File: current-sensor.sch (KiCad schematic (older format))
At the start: 36 parts, among them J1 ‎0197134001‎, J2 ‎0197134001‎, J3 0731000105, J4 Molex_SL_01x02_Male, J5 Molex_SL_01x02_Male, SW1 PN12Sxxx03QE, SW2 OS103011MA7QP1, SW3 OS103011MA7QP1, U1 ACS730xLCTR-40AB, U2 AD8616xRM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

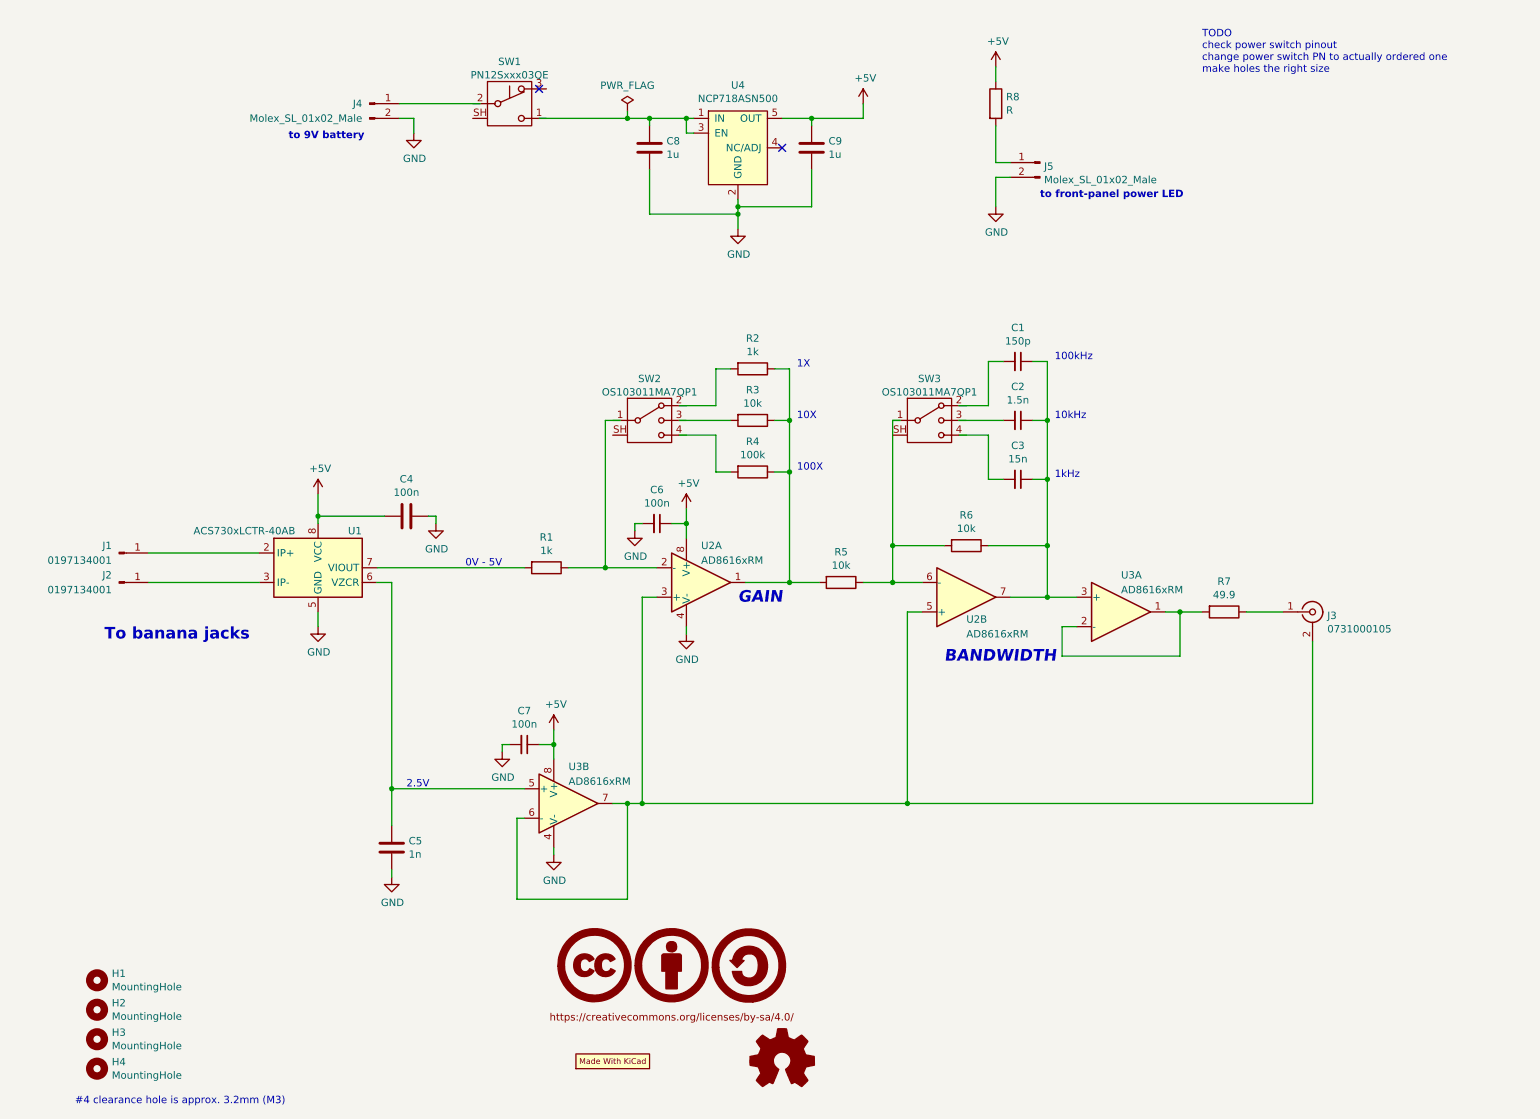
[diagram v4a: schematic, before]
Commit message: complete basic schematic & routing
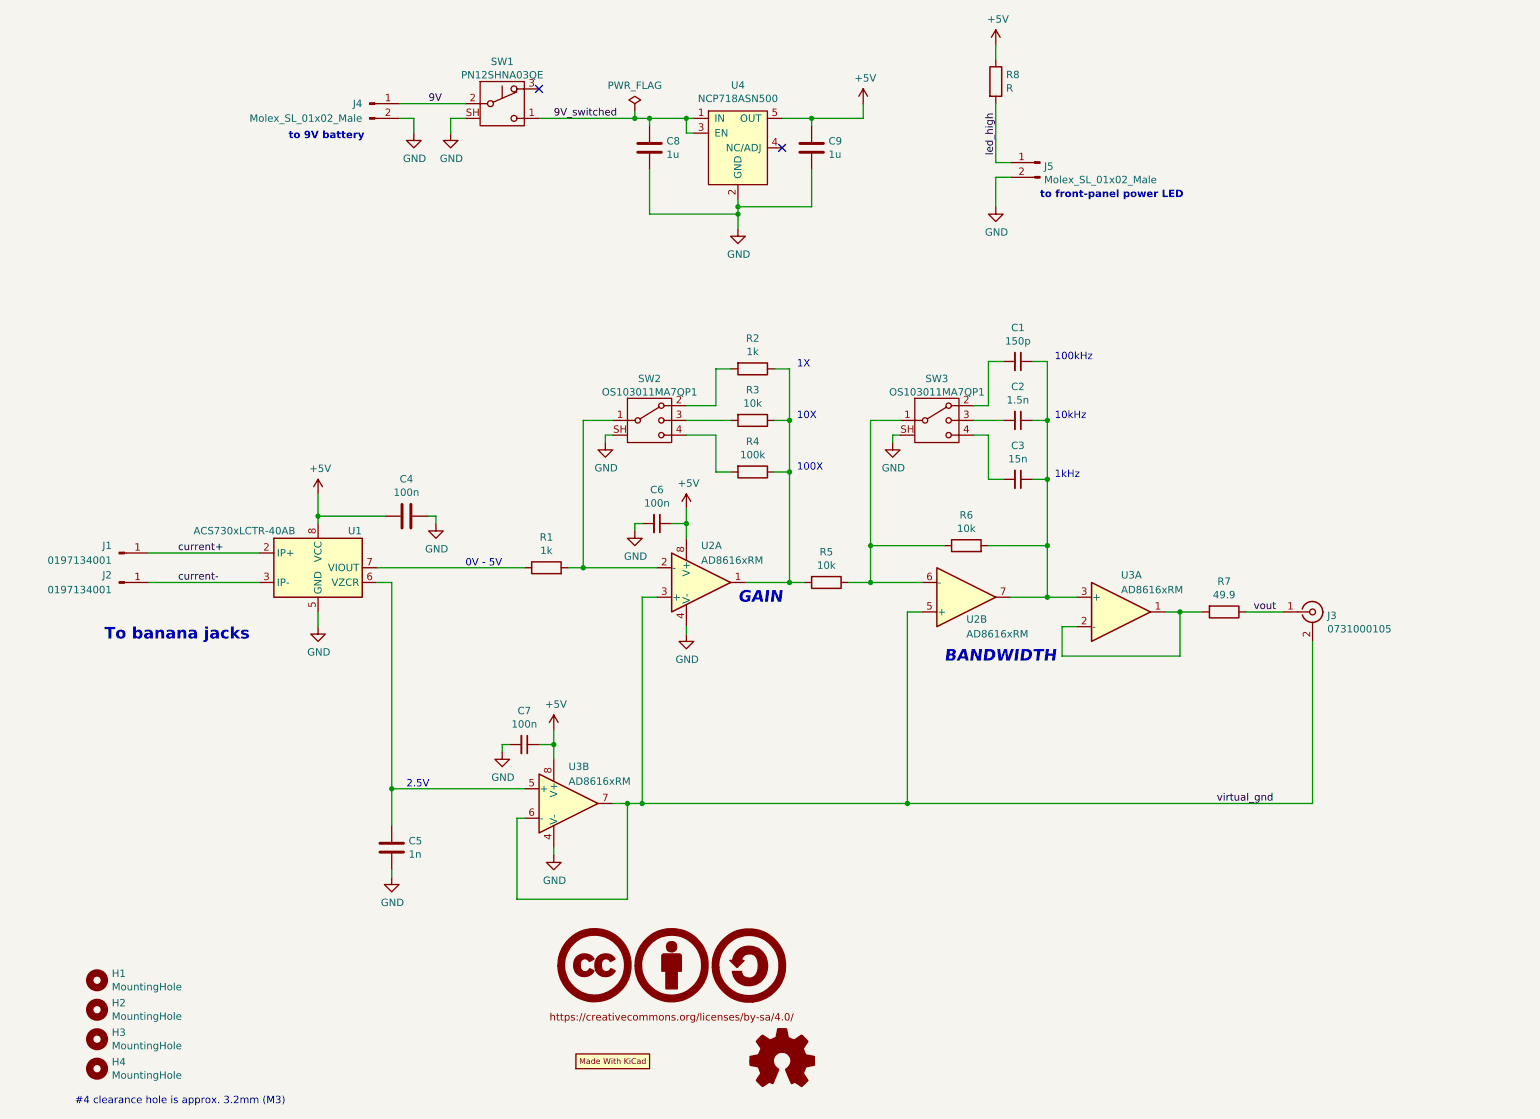
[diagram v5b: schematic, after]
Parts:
- removed U1: ACS730xLCTR-40AB, Package_SO:SOIC-8_3.9x4.9mm_P1.27mm, symbol Sensor_Current_gkeeth:ACS730xLCTR-40AB
- added U1: ACS730xLCTR-40AB, Package_SO:SOIC-8_3.9x4.9mm_P1.27mm, symbol Sensor_Current:ACS730xLCTR-40AB
- SW1: value PN12Sxxx03QE -> PN12SHNA03QE
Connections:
- net labels added: 9V, 9V_switched, current+, current-, led_high, virtual_gnd, vout
- wire segments 115 -> 121
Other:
- note removed: "TODO\ncheck power switch pinout\nchange power switch PN to actually ordered one\nmake holes the right size"
- moved on the sheet: R5, R8, SW1, SW3
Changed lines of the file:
@@
 	1    0    0    -1
 $EndComp
-Text Notes 8600 1000 0    50   ~ 0
-TODO\ncheck power switch pinout\nchange power switch PN to actually ordered one\nmake holes the right size
 $Comp
 L power:+5V #PWR0102
@@
 L power:PWR_FLAG #FLG0101
 U 1 1 5EFBF412
-P 4700 1250
-F 0 "#FLG0101" H 4700 1325 50  0001 C CNN
-F 1 "PWR_FLAG" H 4700 1423 50  0000 C CNN
-F 2 "" H 4700 1250 50  0001 C CNN
-F 3 "~" H 4700 1250 50  0001 C CNN
-	1    4700 1250
-	1    0    0    -1
-$EndComp
-Wire Wire Line
-	4700 1250 4700 1300
+P 4750 1250
+F 0 "#FLG0101" H 4750 1325 50  0001 C CNN
+F 1 "PWR_FLAG" H 4750 1423 50  0000 C CNN
+F 2 "" H 4750 1250 50  0001 C CNN
+F 3 "~" H 4750 1250 50  0001 C CNN
+	1    4750 1250
+	1    0    0    -1
+$EndComp
+Wire Wire Line
+	4750 1250 4750 1300
 $Comp
 L power:GND #PWR0103
@@
 Connection ~ 4850 1300
 Wire Wire Line
-	4850 1300 4700 1300
+	4850 1300 4750 1300
 Wire Wire Line
 	5750 1300 5950 1300
@@
 L Device:R R8
 U 1 1 5EFD8C6E
-P 7200 1200
-F 0 "R8" H 7270 1246 50  0000 L CNN
-F 1 "R" H 7270 1155 50  0000 L CNN
-F 2 "Resistor_SMD:R_0603_1608Metric" V 7130 1200 50  0001 C CNN
-F 3 "~" H 7200 1200 50  0001 C CNN
-	1    7200 1200
+P 7200 1050
+F 0 "R8" H 7270 1096 50  0000 L CNN
+F 1 "R" H 7270 1005 50  0000 L CNN
+F 2 "Resistor_SMD:R_0603_1608Metric" V 7130 1050 50  0001 C CNN
+F 3 "~" H 7200 1050 50  0001 C CNN
+	1    7200 1050
 	1    0    0    -1
 $EndComp
@@
 L power:+5V #PWR0109
 U 1 1 5EFDB3AC
-P 7200 950
-F 0 "#PWR0109" H 7200 800 50  0001 C CNN
-F 1 "+5V" H 7215 1123 50  0000 C CNN
-F 2 "" H 7200 950 50  0001 C CNN
-F 3 "" H 7200 950 50  0001 C CNN
-	1    7200 950
-	1    0    0    -1
-$EndComp
-Wire Wire Line
-	7200 950  7200 1050
+P 7200 800
+F 0 "#PWR0109" H 7200 650 50  0001 C CNN
+F 1 "+5V" H 7215 973 50  0000 C CNN
+F 2 "" H 7200 800 50  0001 C CNN
+F 3 "" H 7200 800 50  0001 C CNN
+	1    7200 800
+	1    0    0    -1
+$EndComp
+Wire Wire Line
+	7200 800  7200 900
 $Comp
 L Amplifier_Operational_gkeeth:AD8616xRM U2
@@
 L Device:R R5
 U 1 1 5EFE0549
-P 6150 4450
-F 0 "R5" V 5943 4450 50  0000 C CNN
-F 1 "10k" V 6034 4450 50  0000 C CNN
-F 2 "Resistor_SMD:R_0603_1608Metric" V 6080 4450 50  0001 C CNN
-F 3 "~" H 6150 4450 50  0001 C CNN
-	1    6150 4450
+P 6050 4450
+F 0 "R5" V 5843 4450 50  0000 C CNN
+F 1 "10k" V 5934 4450 50  0000 C CNN
+F 2 "Resistor_SMD:R_0603_1608Metric" V 5980 4450 50  0001 C CNN
+F 3 "~" H 6050 4450 50  0001 C CNN
+	1    6050 4450
 	0    1    1    0
 $EndComp
@@
 U 1 1 5EFE48EA
 P 7000 4200
-F 0 "R6" V 6793 4200 50  0000 C CNN
-F 1 "10k" V 6884 4200 50  0000 C CNN
+F 0 "R6" V 7207 4200 50  0000 C CNN
+F 1 "10k" V 7116 4200 50  0000 C CNN
 F 2 "Resistor_SMD:R_0603_1608Metric" V 6930 4200 50  0001 C CNN
 F 3 "~" H 7000 4200 50  0001 C CNN
 	1    7000 4200
-	0    1    1    0
-$EndComp
-Wire Wire Line
-	6300 4450 6500 4450
-Wire Wire Line
-	6500 4450 6500 4200
-Wire Wire Line
-	6500 4200 6850 4200
-Connection ~ 6500 4450
-Wire Wire Line
-	6500 4450 6700 4450
+	0    -1   -1   0
+$EndComp
+Wire Wire Line
+	6200 4450 6350 4450
+Wire Wire Line
+	6350 4450 6350 4200
+Wire Wire Line
+	6350 4200 6850 4200
+Connection ~ 6350 4450
+Wire Wire Line
+	6350 4450 6700 4450
 Wire Wire Line
 	7150 4200 7550 4200
@@
 $EndComp
 Wire Wire Line
-	6950 3250 7150 3250
+	7050 3250 7150 3250
 Wire Wire Line
 	7150 3250 7150 2950
@@
 	7150 2950 7250 2950
 Wire Wire Line
-	6950 3350 7250 3350
-Wire Wire Line
-	6950 3450 7150 3450
+	7050 3350 7250 3350
+Wire Wire Line
+	7050 3450 7150 3450
 Wire Wire Line
 	7150 3450 7150 3750
@@
 	7150 3750 7250 3750
 Wire Wire Line
-	6500 4200 6500 3350
-Wire Wire Line
-	6500 3350 6550 3350
-Connection ~ 6500 4200
+	6350 4200 6350 3350
+Wire Wire Line
+	6350 3350 6550 3350
+Connection ~ 6350 4200
 Wire Wire Line
 	7550 3750 7450 3750
@@
 U 1 1 5F007FE6
 P 4150 4350
-F 0 "R1" V 3943 4350 50  0000 C CNN
-F 1 "1k" V 4034 4350 50  0000 C CNN
+F 0 "R1" V 4357 4350 50  0000 C CNN
+F 1 "1k" V 4266 4350 50  0000 C CNN
 F 2 "Resistor_SMD:R_0603_1608Metric" V 4080 4350 50  0001 C CNN
 F 3 "~" H 4150 4350 50  0001 C CNN
 	1    4150 4350
-	0    1    1    0
+	0    -1   -1   0
 $EndComp
 $Comp
@@
 	5300 3000 5300 3250
 Wire Wire Line
-	5300 3250 5050 3250
-Wire Wire Line
-	5050 3350 5400 3350
-Wire Wire Line
-	5050 3450 5300 3450
+	5300 3250 5100 3250
+Wire Wire Line
+	5100 3350 5400 3350
+Wire Wire Line
+	5100 3450 5300 3450
 Wire Wire Line
 	5300 3450 5300 3700
@@
 	5300 3700 5400 3700
 Wire Wire Line
-	4650 3350 4550 3350
-Wire Wire Line
-	4550 3350 4550 4350
-Wire Wire Line
-	4550 4350 4900 4350
+	4600 3350 4400 3350
+Wire Wire Line
+	4400 4350 4900 4350
 Wire Wire Line
 	5500 4450 5800 4450
@@
 	5800 3700 5800 3350
 Wire Wire Line
-	4300 4350 4550 4350
-Connection ~ 4550 4350
+	4300 4350 4400 4350
+Connection ~ 4400 4350
 Text Notes 5850 3000 0    50   ~ 0
 1X
@@
 	3100 5850 3100 6100
 Wire Wire Line
-	6000 4450 5800 4450
+	5900 4450 5800 4450
 Connection ~ 5800 4450
 $Comp
@@
 $EndComp
 $Comp
-L Sensor_Current_gkeeth:ACS730xLCTR-40AB U1
-U 1 1 5F083F8B
-P 2600 4350
-F 0 "U1" H 2850 4600 50  0000 C CNN
-F 1 "ACS730xLCTR-40AB" H 2100 4600 50  0000 C CNN
-F 2 "Package_SO:SOIC-8_3.9x4.9mm_P1.27mm" H 2950 4250 50  0001 L CIN
-F 3 "http://www.allegromicro.com/~/media/Files/Datasheets/ACS730-Datasheet.ashx?la=en" H 2600 4350 50  0001 C CNN
-	1    2600 4350
-	1    0    0    -1
-$EndComp
-$Comp
 L Regulator_Linear_gkeeth:NCP718ASN500 U4
 U 1 1 5F257D76
@@
 NoConn ~ 4100 1100
 Wire Wire Line
-	3150 1200 3700 1200
-Connection ~ 4700 1300
-Wire Wire Line
-	4100 1300 4700 1300
+	3150 1200 3600 1200
+Connection ~ 4750 1300
 $Comp
 L Connector:Conn_Coaxial J3
@@
 L Switch_gkeeth:PN12Sxxx03QE SW1
 U 1 1 5F261DB5
-P 3900 1200
-F 0 "SW1" H 3900 1485 50  0000 C CNN
-F 1 "PN12Sxxx03QE" H 3900 1394 50  0000 C CNN
-F 2 "Button_Switch_THT_gkeeth:SW_Push_SPDT_CK_PN1xSxxx03QE" H 3900 1200 50  0001 C CNN
-F 3 "https://www.ckswitches.com/media/1413/pn.pdf" H 3900 1200 50  0001 C CNN
-	1    3900 1200
-	1    0    0    -1
-$EndComp
-$Comp
-L Switch_gkeeth:OS103011MA7QP1 SW2
-U 1 1 5F2627B8
-P 4850 3350
-F 0 "SW2" H 4850 3633 50  0000 C CNN
-F 1 "OS103011MA7QP1" H 4850 3542 50  0000 C CNN
-F 2 "Button_Switch_THT_gkeeth:SW_Slide_SP3T_CK_OS103011MA7QP1" H 4225 3525 50  0001 C CNN
-F 3 "https://www.ckswitches.com/media/1428/os.pdf" H 4225 3525 50  0001 C CNN
-	1    4850 3350
+P 3850 1200
+F 0 "SW1" H 3850 1485 50  0000 C CNN
+F 1 "PN12SHNA03QE" H 3850 1394 50  0000 C CNN
+F 2 "Button_Switch_THT_gkeeth:SW_Push_SPDT_CK_PN1xSxxx03QE" H 3850 1200 50  0001 C CNN
+F 3 "https://www.ckswitches.com/media/1413/pn.pdf" H 3850 1200 50  0001 C CNN
+	1    3850 1200
 	1    0    0    -1
 $EndComp
@@
 L Switch_gkeeth:OS103011MA7QP1 SW3
 U 1 1 5F26317F
-P 6750 3350
-F 0 "SW3" H 6750 3633 50  0000 C CNN
-F 1 "OS103011MA7QP1" H 6750 3542 50  0000 C CNN
-F 2 "Button_Switch_THT_gkeeth:SW_Slide_SP3T_CK_OS103011MA7QP1" H 6125 3525 50  0001 C CNN
-F 3 "https://www.ckswitches.com/media/1428/os.pdf" H 6125 3525 50  0001 C CNN
-	1    6750 3350
+P 6800 3350
+F 0 "SW3" H 6800 3633 50  0000 C CNN
+F 1 "OS103011MA7QP1" H 6800 3542 50  0000 C CNN
+F 2 "Button_Switch_THT_gkeeth:SW_Slide_SP3T_CK_OS103011MA7QP1" H 6175 3525 50  0001 C CNN
+F 3 "https://www.ckswitches.com/media/1428/os.pdf" H 6175 3525 50  0001 C CNN
+	1    6800 3350
 	1    0    0    -1
 $EndComp
@@
 	7200 1600 7300 1600
 Wire Wire Line
-	7200 1350 7200 1600
-Wire Wire Line
 	7300 1700 7200 1700
 Wire Wire Line
@@
 	1    0    0    -1
 $EndComp
+Text Label 1650 4250 0    50   ~ 0
+current+
+Text Label 1650 4450 0    50   ~ 0
+current-
+Text Label 8950 4650 0    50   ~ 0
+vout
+Text Label 8700 5950 0    50   ~ 0
+virtual_gnd
+Text Label 3350 1200 0    50   ~ 0
+9V
+Text Label 4200 1300 0    50   ~ 0
+9V_switched
+Text Label 7200 1550 1    50   ~ 0
+led_high
+Wire Wire Line
+	7200 1200 7200 1600
+$Comp
+L Sensor_Current:ACS730xLCTR-40AB U1
+U 1 1 5F43380D
+P 2600 4350
+F 0 "U1" H 2850 4600 50  0000 C CNN
+F 1 "ACS730xLCTR-40AB" H 2100 4600 50  0000 C CNN
+F 2 "Package_SO:SOIC-8_3.9x4.9mm_P1.27mm" H 2950 4250 50  0001 L CIN
+F 3 "http://www.allegromicro.com/~/media/Files/Datasheets/ACS730-Datasheet.ashx?la=en" H 2600 4350 50  0001 C CNN
+	1    2600 4350
+	1    0    0    -1
+$EndComp
+Wire Wire Line
+	4100 1300 4750 1300
+$Comp
+L power:GND #PWR0116
+U 1 1 5F456228
+P 3500 1400
+F 0 "#PWR0116" H 3500 1150 50  0001 C CNN
+F 1 "GND" H 3505 1227 50  0000 C CNN
+F 2 "" H 3500 1400 50  0001 C CNN
+F 3 "" H 3500 1400 50  0001 C CNN
+	1    3500 1400
+	1    0    0    -1
+$EndComp
+Wire Wire Line
+	3500 1400 3500 1300
+Wire Wire Line
+	3500 1300 3600 1300
+Wire Wire Line
+	4400 3350 4400 4350
+$Comp
+L Switch_gkeeth:OS103011MA7QP1 SW2
+U 1 1 5F2627B8
+P 4850 3350
+F 0 "SW2" H 4850 3633 50  0000 C CNN
+F 1 "OS103011MA7QP1" H 4850 3542 50  0000 C CNN
+F 2 "Button_Switch_THT_gkeeth:SW_Slide_SP3T_CK_OS103011MA7QP1" H 4225 3525 50  0001 C CNN
+F 3 "https://www.ckswitches.com/media/1428/os.pdf" H 4225 3525 50  0001 C CNN
+	1    4850 3350
+	1    0    0    -1
+$EndComp
+$Comp
+L power:GND #PWR0117
+U 1 1 5F47592F
+P 4550 3500
+F 0 "#PWR0117" H 4550 3250 50  0001 C CNN
+F 1 "GND" H 4555 3327 50  0000 C CNN
+F 2 "" H 4550 3500 50  0001 C CNN
+F 3 "" H 4550 3500 50  0001 C CNN
+	1    4550 3500
+	1    0    0    -1
+$EndComp
+Wire Wire Line
+	4550 3500 4550 3450
+Wire Wire Line
+	4550 3450 4600 3450
+$Comp
+L power:GND #PWR0118
+U 1 1 5F495411
+P 6500 3500
+F 0 "#PWR0118" H 6500 3250 50  0001 C CNN
+F 1 "GND" H 6505 3327 50  0000 C CNN
+F 2 "" H 6500 3500 50  0001 C CNN
+F 3 "" H 6500 3500 50  0001 C CNN
+	1    6500 3500
+	1    0    0    -1
+$EndComp
+Wire Wire Line
+	6500 3500 6500 3450
+Wire Wire Line
+	6500 3450 6550 3450
 $EndSCHEMATC
